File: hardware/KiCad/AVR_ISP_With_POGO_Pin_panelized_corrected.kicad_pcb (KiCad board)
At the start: 2 copper layers, 93.6 x 85.5 mm, 521 parts, among them P1 75869-131LF, P2 P50-B1

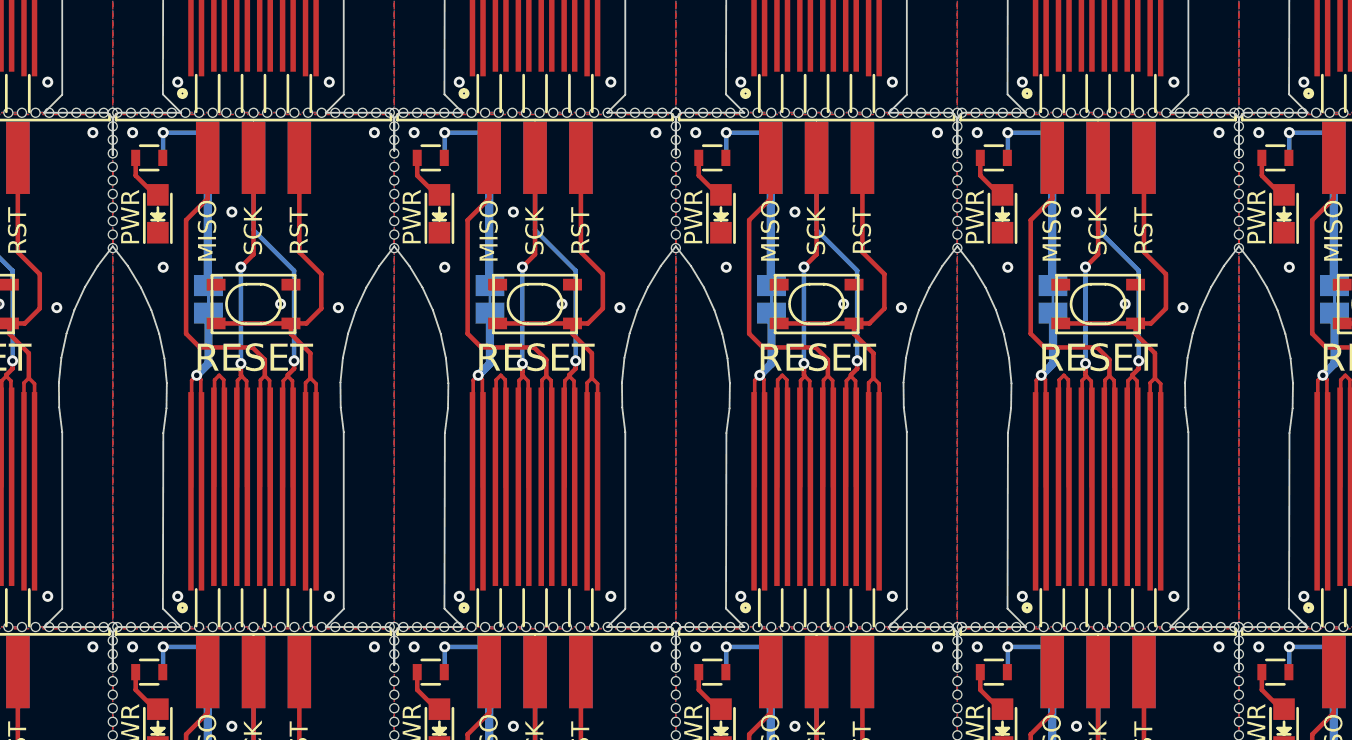
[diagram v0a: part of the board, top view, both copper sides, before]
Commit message: Panelized with Mousebites
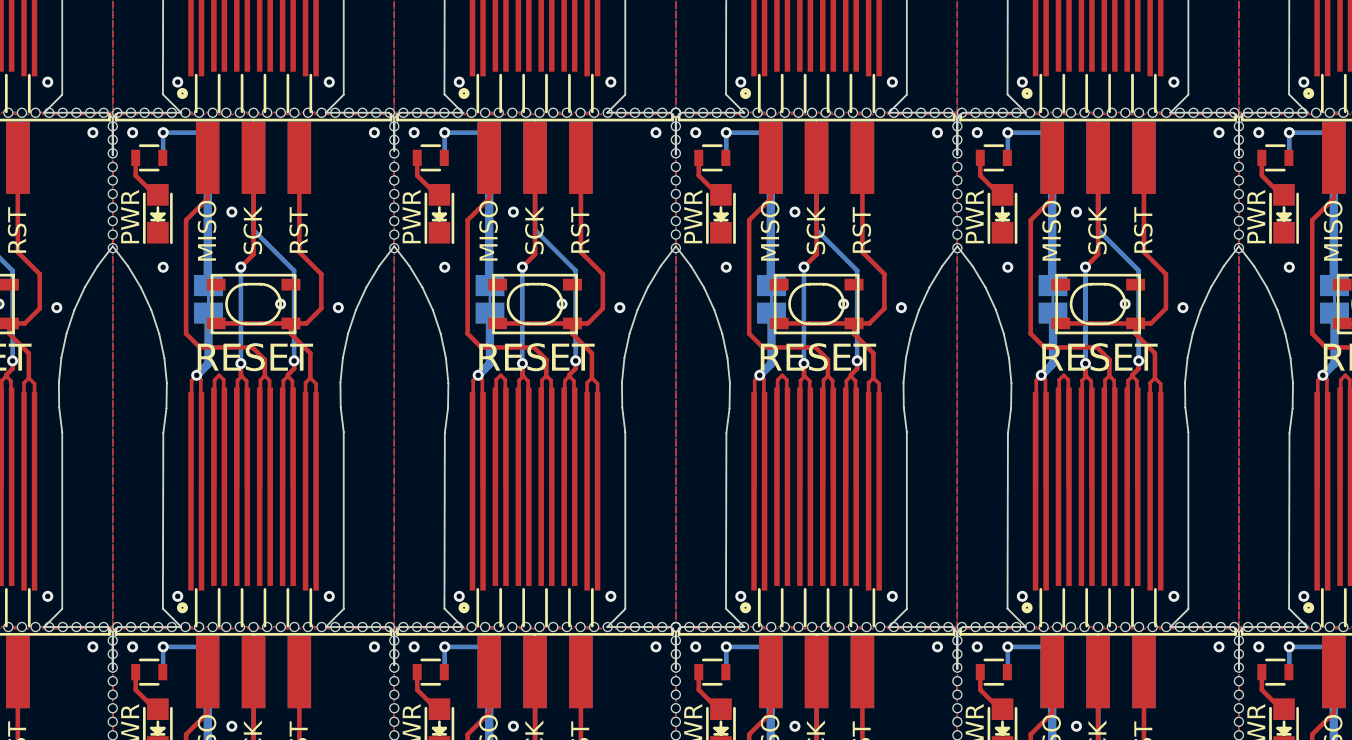
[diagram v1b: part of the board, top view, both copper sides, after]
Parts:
- removed the REF** at (81.2, 78.5)
- removed the REF** at (128.0, 78.5)
- removed the REF** at (81.2, 107.0)
- removed the REF** at (65.6, 78.5)
- removed the REF** at (65.6, 107.0)
- removed the REF** at (128.0, 107.0)
- removed the REF** at (112.4, 78.5)
- removed the REF** at (112.4, 107.0)
